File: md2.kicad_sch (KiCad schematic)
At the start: 44 parts, among them IC1 TC74HC4066AP_F_, IC2 TC74HC4066AP_F_, IC3 TC74HC04AP, IC4 TB6643KQ, IC5 TB6643KQ, IC6 TB6643KQ, IC7 TB6643KQ, J1 Conn_01x02_Pin, J10 Conn_01x02_Pin, J3 Conn_02x13_Odd_Even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

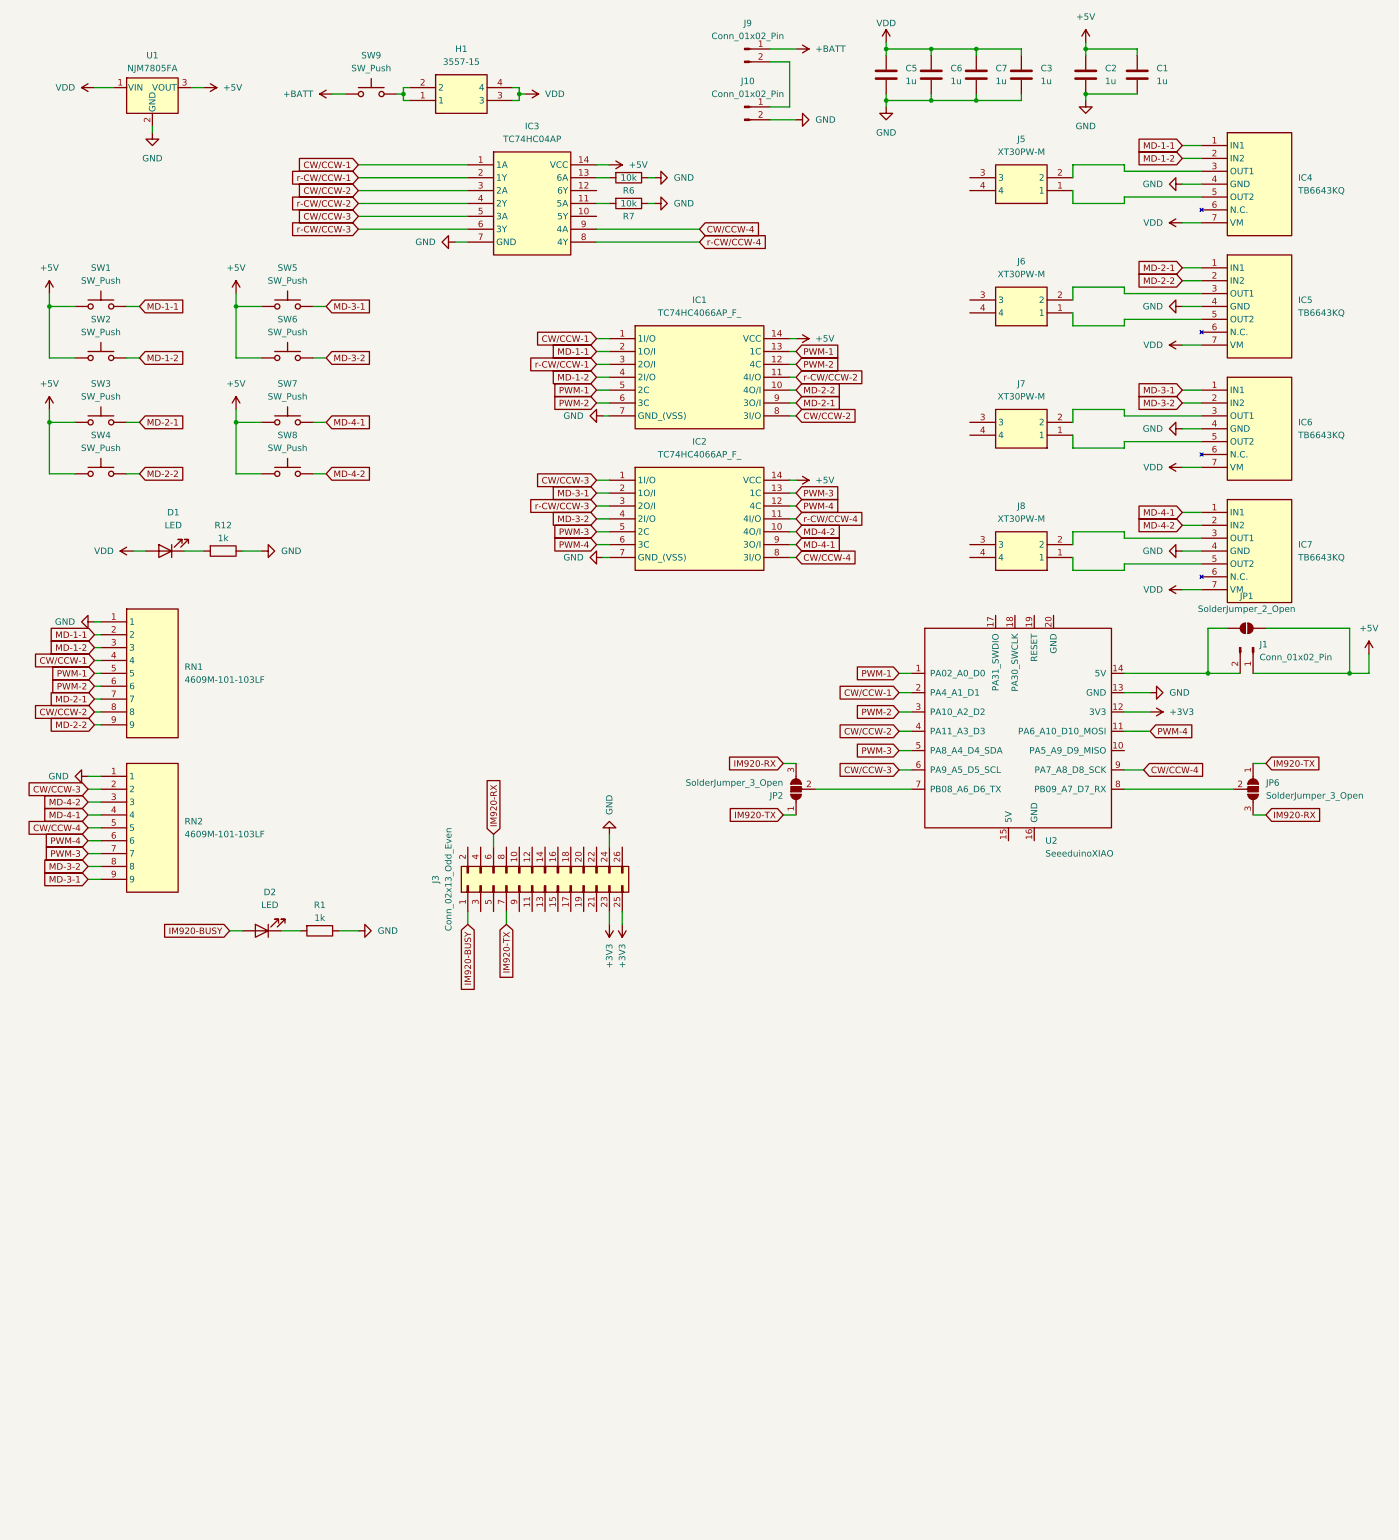
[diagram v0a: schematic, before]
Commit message: support survo motor
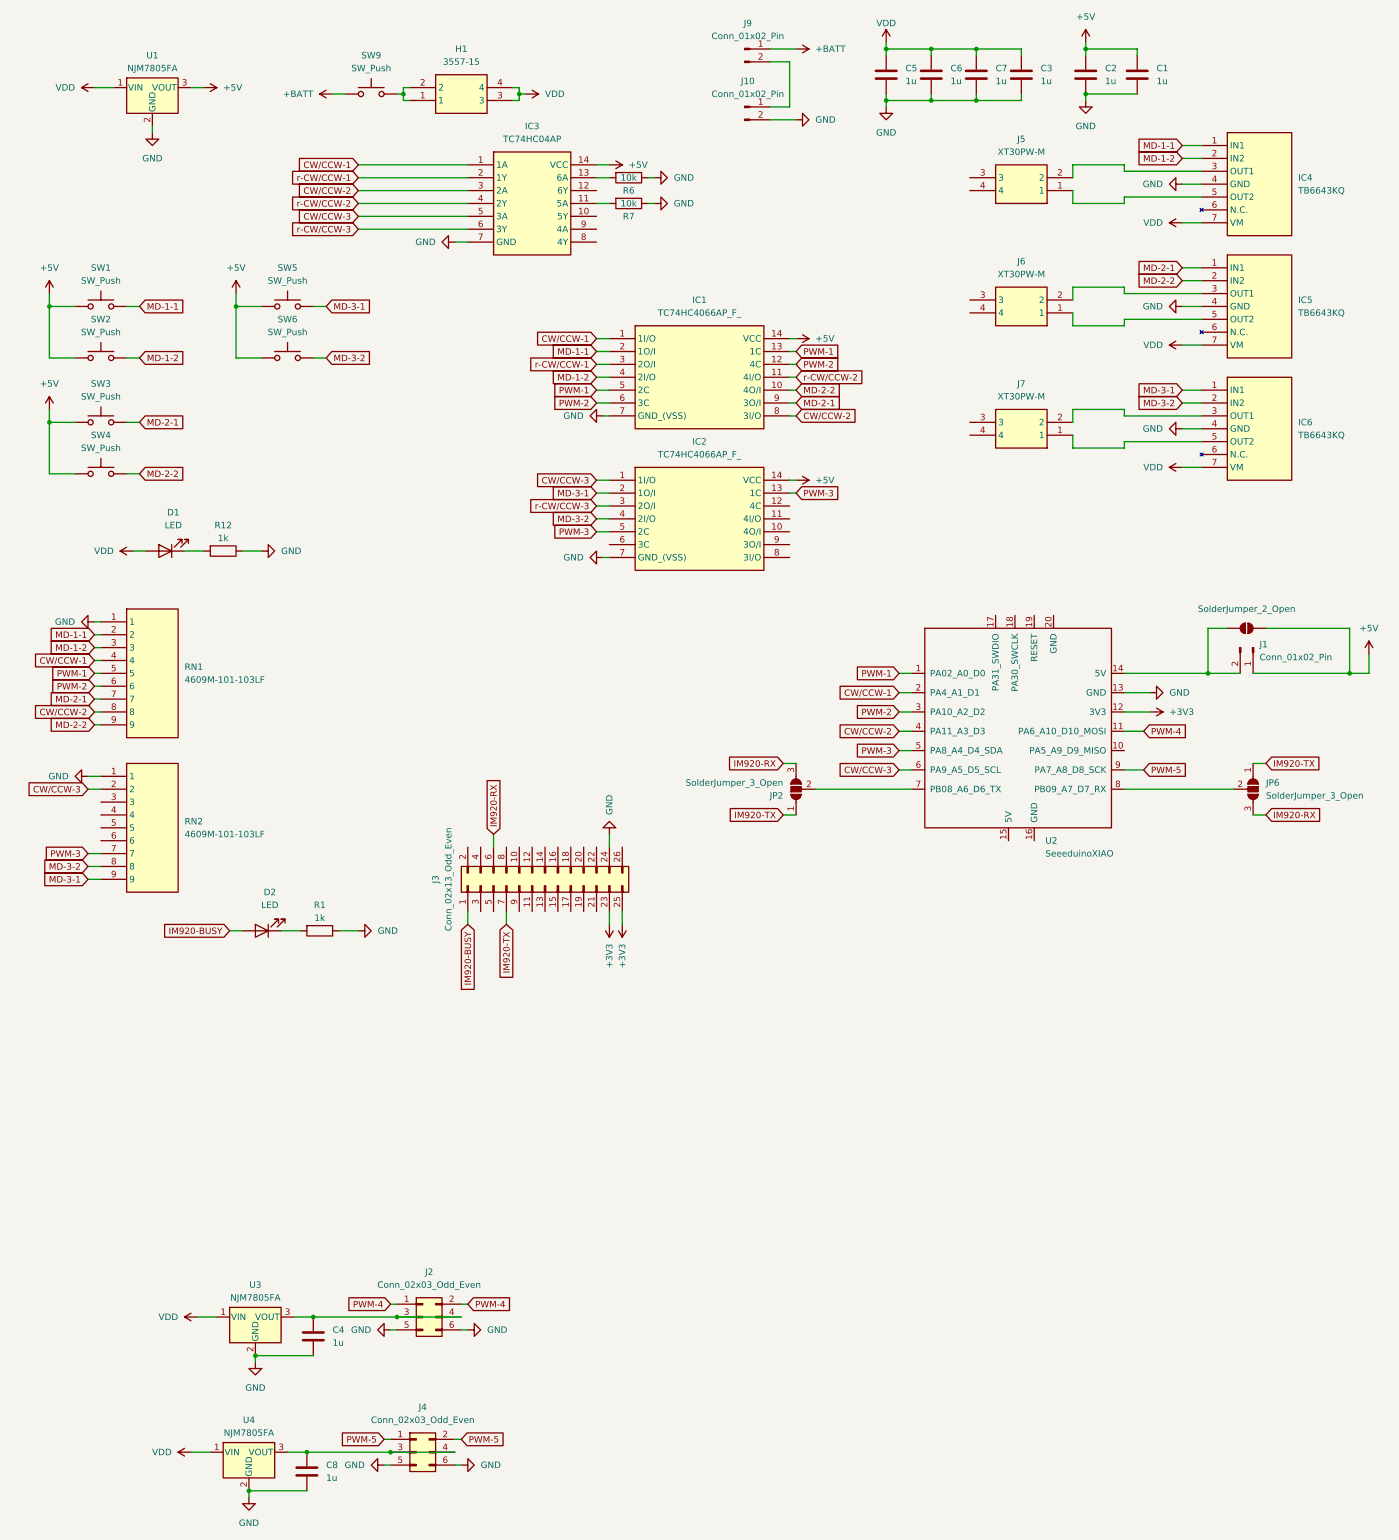
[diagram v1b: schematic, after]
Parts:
- removed IC7: TB6643KQ, TB6643KQ:TB6643KQ, symbol TB6643KQ:TB6643KQ
- removed J8: XT30PW-M, XT30PW-M:XT30PWM, symbol XT30PW-M:XT30PW-M
- removed SW7, SW8: SW_Push, Button_Switch_THT:SW_PUSH_6mm, symbol Switch:SW_Push
- added C4, C8: 1u, Capacitor_THT:C_Disc_D6.0mm_W4.4mm_P5.00mm, symbol Device:C
- added J2, J4: Conn_02x03_Odd_Even, Connector_PinSocket_2.54mm:PinSocket_2x03_P2.54mm_Vertical, symbol Connector_Generic:Conn_02x03_Odd_Even
- added U3, U4: NJM7805FA, Connector_PinSocket_2.54mm:PinSocket_1x03_P2.54mm_Vertical, symbol Regulator_Linear:AP2204R-3.0
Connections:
- net GND: now also C4.2, C8.2, J2.5 (Pin_5), J2.6 (Pin_6), J4.5 (Pin_5), J4.6 (Pin_6), U3.2 (GND), U4.2 (GND)
- net PWM-4: now also J2.1 (Pin_1), J2.2 (Pin_2); no longer IC2.12 (4C), IC2.6 (3C), RN2.6
- net VDD: now also U3.1 (VIN), U4.1 (VIN)
- removed net CW/CCW-4: IC2.8 (3I/O), IC3.9 (4A), RN2.5, U2.9 (PA7_A8_D8_SCK)
- net MD-4-1: no longer names the net of RN2.4
- net MD-4-1: no longer IC2.9 (3O/I)
- net MD-4-2: no longer names the net of RN2.3
- net MD-4-2: no longer IC2.10 (4O/I)
- net r-CW/CCW-4: no longer names the net of IC3.8 (4Y)
- net r-CW/CCW-4: no longer IC2.11 (4I/O)
- new net: C8.1, J4.3 (Pin_3), J4.4 (Pin_4), U4.3 (VOUT)
- new net: C4.1, J2.3 (Pin_3), J2.4 (Pin_4), U3.3 (VOUT)
- new net PWM-5: J4.1 (Pin_1), J4.2 (Pin_2), U2.9 (PA7_A8_D8_SCK)
